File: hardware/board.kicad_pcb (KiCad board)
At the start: 2 copper layers, 65 x 140 mm, 25 parts, among them P1 CONN_4, P2 CONN_6, P3 CONN_6, Q1 BC547, U1 PIC16F628A, U2 7805

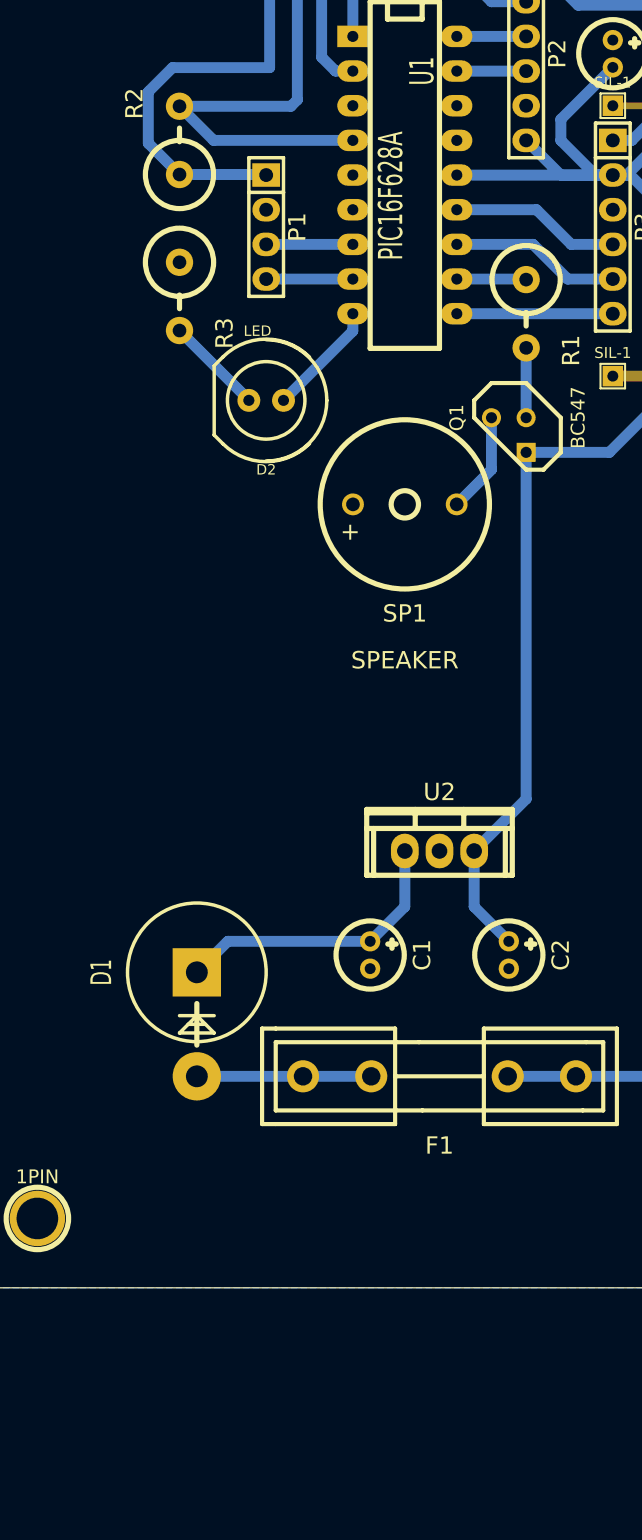
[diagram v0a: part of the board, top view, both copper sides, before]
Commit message: JZ: Label everything + ugly power tag workaround
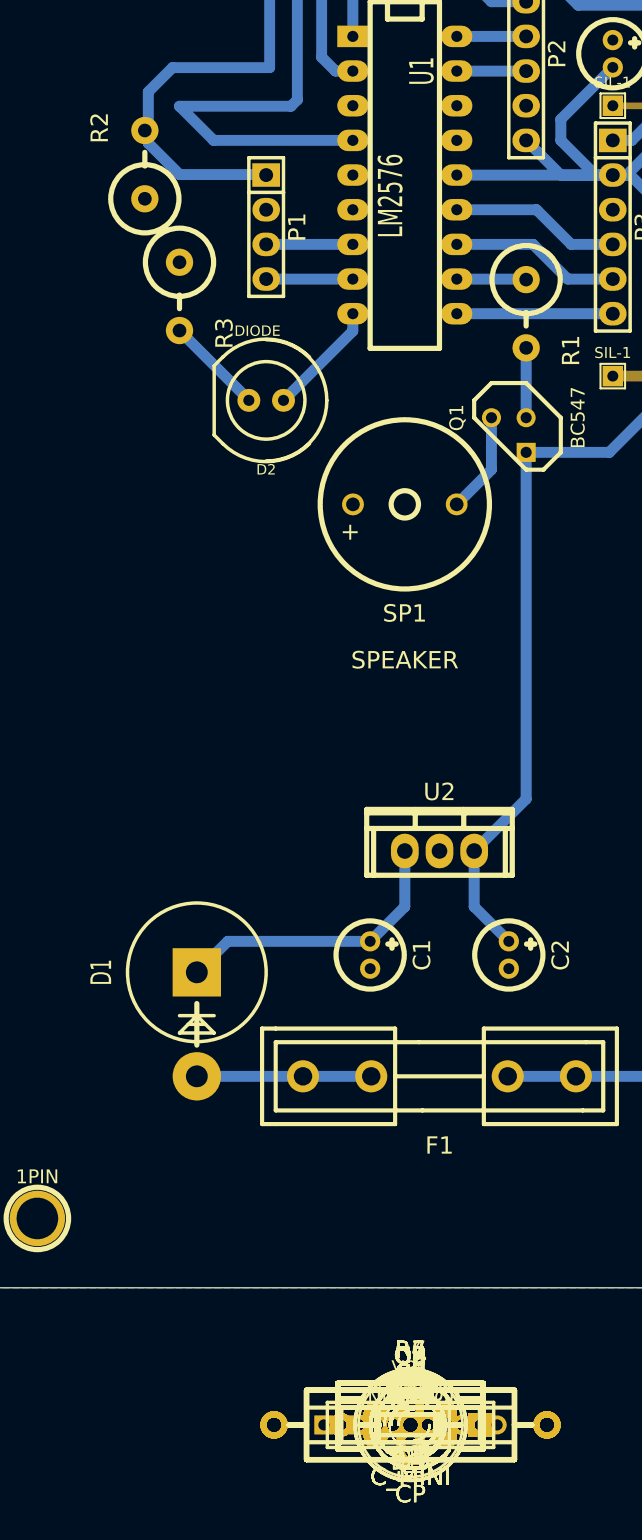
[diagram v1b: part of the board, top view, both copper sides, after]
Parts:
- added BT1: CONN_4, Connect:SIL-4, F.Cu at (147.7, 174.1)
- added C4, C5, C6, C7: C_MINI, Capacitors_ThroughHole:Capacitor5x11RM2.5, F.Cu at (147.7, 174.1)
- added C8, C9: CP, Capacitors_ThroughHole:Capacitor8x13RM3.8, F.Cu at (147.7, 174.1)
- added D10, D11, D12, D13, D14, D6, D7, D8, D9: LED, LEDs:LED-5MM, F.Cu at (147.7, 174.1)
- added D15, D16, D17, D18, D3, D4: DIODE, Diodes_ThroughHole:Diode_DO-35_SOD27_Horizontal_RM10, F.Cu at (147.7, 174.1)
- added D5: DIODESCH, Diodes_ThroughHole:Diode_DO-35_SOD27_Horizontal_RM10, F.Cu at (147.7, 174.1)
- added L1: INDUCTOR, Inductors:INDUCTOR_V, F.Cu at (147.7, 174.1)
- added Pickit3: CONN_6, Connect:SIL-6, F.Cu at (147.7, 174.1)
- added Q2, Q3, Q4, Q5: RFP50N06, Transistors_TO-220:TO-220_FET-GDS_Vertical_LargePads, F.Cu at (147.7, 174.1)
- added R4, R5, R6, R7: R, Resistors_ThroughHole:Resistor_Horizontal_RM20mm, F.Cu at (147.7, 174.1)
- added U3: LM7810ACT, Transistors_TO-220:TO-220_FET-GDS_Vertical_MountedFromLS_LargePads, F.Cu at (147.7, 174.1)
- added VR1: VR, Capacitors_ThroughHole:Capacitor12MMDiscRM7.75, F.Cu at (147.7, 174.1)
- C1: value 100nF -> 100uF
- C2: value 100nF -> 6800uF
- D1: value 1N007 -> DIODE
- D2: value LED -> DIODE
- F1: value 0.16A -> 1A
- P1: value CONN_4 -> SCREW TERM 1
- P2: value CONN_6 -> SCREW TERM 2
- P3: value CONN_6 -> SCREW TERM 3
- U1: value PIC16F628A -> LM2576
- U2: value 7805 -> PIC16F628A
- moved R2 3.10 mm to (128.3, 81.8)
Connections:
- C1 pad 1: N-000024 -> Net-(C1-Pad1)
- C1 pad 2: GND -> DGND
- C2 pad 2: GND -> DGND
- C3 pad 1: GND -> DGND
- D1 pad 1: N-000023 -> AGND
- D1 pad 2: N-000024 -> Net-(C1-Pad1)
- D2 pad 1: /LED -> Net-(D2-Pad1)
- D2 pad 2: N-000019 -> Net-(C1-Pad1)
- F1 pad 1: +12V -> /S0_I
- F1 pad 2: N-000023 -> Net-(D2-Pad1)
- P1 pad 1: +5V -> /S0_I
- P1 pad 2: GND -> /S0_O
- P1 pad 3: /P1_RX -> /S1_I
- P1 pad 4: /P1_TX -> (no net)
- P2 pad 1: N-000014 -> /S1_O
- P2 pad 2: N-000006 -> /S2_I
- P2 pad 3: N-000002 -> /S2_O
- P2 pad 4: N-000003 -> (no net)
- P2 pad 5: GND -> (no net)
- P2 pad 6: +5V -> (no net)
- P3 pad 1: /P3_1 -> /S3_I
- P3 pad 2: +5V -> /S3_O
- P3 pad 3: GND -> AGND
- P3 pad 4: /P3_4 -> (no net)
- P3 pad 5: /P3_5 -> (no net)
- P3 pad 6: /P3_6 -> (no net)
- R2 pad 2: /P3_1 -> /PK3_1
- R3 pad 1: GND -> DGND
- R3 pad 2: N-000019 -> Net-(D6-Pad2)
- SP1 pad 2: GND -> DGND
- U1 pad 1: N-000006 -> Net-(C1-Pad1)
- U1 pad 10: /P3_6 -> (no net)
- U1 pad 11: /BZR -> (no net)
- U1 pad 12: /P3_5 -> (no net)
- U1 pad 13: /P3_4 -> (no net)
- U1 pad 14: +5V -> (no net)
- U1 pad 17: N-000003 -> (no net)
- U1 pad 18: N-000002 -> (no net)
- U1 pad 2: N-000014 -> Net-(D5-Pad2)
- U1 pad 3: (no net) -> DGND
- U1 pad 4: /P3_1 -> +5V
- U1 pad 5: GND -> DGND
- U1 pad 7: /P1_RX -> (no net)
- U1 pad 8: /P1_TX -> (no net)
- U1 pad 9: /LED -> (no net)
- U2 pad GND: GND -> (no net)
- U2 pad VI: N-000024 -> (no net)
- U2 pad VO: +5V -> (no net)
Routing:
- net +5V: track 188.4 -> 96.6 mm
- net /PK3_1: track 0.00 -> 85.0 mm
- net /P3_1: track 77.3 -> 0.00 mm
- net /S3_I: track 0.00 -> 55.4 mm
- net (no net): track 0.00 -> 52.9 mm
- net Net-(C1-Pad1): track 0.00 -> 37.6 mm
- net N-000014: track 24.7 -> 0.00 mm
- net N-000024: track 23.1 -> 0.00 mm
- net /S3_O: track 0.00 -> 22.4 mm
- net /S0_I: track 0.00 -> 18.9 mm
- net N-000006: track 17.0 -> 0.00 mm
- net /S1_O: track 0.00 -> 15.4 mm
- net Net-(D2-Pad1): track 0.00 -> 13.5 mm
- net N-000023: track 12.8 -> 0.00 mm
- net +12V: track 12.5 -> 0.00 mm
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
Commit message: Heavily modded pcb + New footprint associations
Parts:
- removed 1PIN (x4): P***, Connect:1pin
- removed SIL-1 (x4): Val**, Connect:SIL-1
- removed SIL-2: Val**, Connect:SIL-2
- added IC1: PC817, opto:DIP-4__300, F.Cu at (210.8, 121.9)
- added IC2: PC817, opto:DIP-4__300, F.Cu at (198.1, 121.9)
- added IC3: PC817, opto:DIP-4__300, F.Cu at (232.4, 121.9)
- added IC4: PC817, opto:DIP-4__300, F.Cu at (219.7, 121.9)
- added IC5: PC817, opto:DIP-4__300, F.Cu at (222.2, 86.4)
- added IC6: PC817, opto:DIP-4__300, F.Cu at (234.9, 86.4)
- added IC7: PC817, opto:DIP-4__300, F.Cu at (200.7, 86.4)
- added IC8: PC817, opto:DIP-4__300, F.Cu at (213.4, 86.4)
- BT1: footprint Connect:SIL-4 -> Pin_Headers:Pin_Header_Straight_1x04
- C1: footprint Capacitors_Elko_ThroughHole:Elko_vert_DM5_RM2 -> Capacitors_ThroughHole:Capacitor10x25RM2.5
- C2: footprint Capacitors_Elko_ThroughHole:Elko_vert_DM5_RM2 -> Capacitors_ThroughHole:Capacitor16x25RM7.5
- C3: footprint Capacitors_Elko_ThroughHole:Elko_vert_DM5_RM2 -> Capacitors_ThroughHole:Capacitor3MMDiscRM2.5
- D1: footprint Diodes_ThroughHole:Diode_P600_Vertical_AnodeUp -> Diodes_ThroughHole:Diode_DO-41_SOD81_Vertical_AnodeUp
- D15, D16, D17, D18, D3, D4, D5: footprint Diodes_ThroughHole:Diode_DO-35_SOD27_Horizontal_RM10 -> Diodes_ThroughHole:Diode_DO-41_SOD81_Vertical_AnodeUp
- D2: footprint LEDs:LED-8MM -> Diodes_ThroughHole:Diode_DO-41_SOD81_Vertical_AnodeUp
- F1: footprint Fuse_Holders_and_Fuses:Fuseholder5x20_horiz_open_inline_Type-I -> Fuse_Holders_and_Fuses:Fuseholder5x20_horiz_SemiClosed_Casing10x25mm
- P1: footprint Pin_Headers:Pin_Header_Straight_1x04 -> moje's kicad footprints:Sawatronix_screwterm3
- P2, P3: footprint Pin_Headers:Pin_Header_Straight_1x06 -> moje's kicad footprints:Sawatronix_screwterm3
- Pickit3: footprint Connect:SIL-6 -> Pin_Headers:Pin_Header_Straight_1x06
- R1: footprint Resistors_ThroughHole:Resistor_Vertical_RM5mm -> Resistors_ThroughHole:Resistor_Horizontal_RM10mm
- R3: footprint Resistors_ThroughHole:Resistor_Vertical_RM5mm -> Resistors_ThroughHole:Resistor_Horizontal_RM15mm
- R4, R5, R6, R7: footprint Resistors_ThroughHole:Resistor_Horizontal_RM20mm -> Resistors_ThroughHole:Resistor_Vertical_RM5mm
- SP1: footprint Buzzers_Beepers:MagneticBuzzer_ProSignal_ABI-009-RC -> Buzzers_Beepers:MagneticBuzzer_ProSignal_ABT-410-RC
- U1: footprint Sockets_DIP:DIP-18__300_ELL -> Pentawatts:Pentawatt_Neutral_Straight_Vertical_TO220-5-T05A
- U2: footprint moje's kicad footprints:78XX -> Sockets_DIP:DIP-18__300_ELL
- U3: value LM7810ACT -> LM7810; footprint Transistors_TO-220:TO-220_FET-GDS_Vertical_MountedFromLS_LargePads -> moje's kicad footprints:78XX
- VR1: footprint Capacitors_ThroughHole:Capacitor12MMDiscRM7.75 -> Capacitors_ThroughHole:Capacitor6MMDiscRM5
- moved D17 129.3 mm to (234.9, 78.7)
- moved Q4 129.2 mm to (227.3, 72.4)
- moved C6 124.2 mm to (227.3, 78.7), turned to 270 degrees
- moved Q5 117.1 mm to (205.7, 72.4)
- moved D12 115.8 mm to (233.7, 96.5), turned to 270 degrees
- moved D18 115.8 mm to (213.4, 78.7)
- moved P1 114.9 mm to (246.4, 121.9)
- moved R6 113.9 mm to (227.3, 92.7), turned to 270 degrees
- moved C7 111.6 mm to (205.7, 78.7), turned to 270 degrees
- moved D11 106.7 mm to (221.0, 96.5), turned to 90 degrees
- moved D9 106.2 mm to (233.7, 111.8), turned to 270 degrees
- moved D14 100.8 mm to (212.1, 96.5), turned to 270 degrees
- moved R7 100.0 mm to (205.7, 92.7), turned to 270 degrees
- moved L1 99.4 mm to (173.4, 78.1)
- moved R5 98.8 mm to (227.3, 115.6), turned to 90 degrees
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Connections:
- C8 pad 1: Net-(C8-Pad1) -> /S0_I
- Q2 pad D: (no net) -> /S0_I
- Q2 pad G: (no net) -> Net-(IC1-Pad4)
- Q2 pad S: (no net) -> /S0_O
- Q3 pad D: (no net) -> /S1_I
- Q3 pad G: (no net) -> Net-(IC3-Pad4)
- Q3 pad S: (no net) -> /S1_O
- Q4 pad D: (no net) -> /S2_I
- Q4 pad G: (no net) -> Net-(IC5-Pad4)
- Q4 pad S: (no net) -> /S2_O
- Q5 pad D: (no net) -> /S3_I
- Q5 pad G: (no net) -> Net-(IC7-Pad4)
- Q5 pad S: (no net) -> /S3_O
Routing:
- net AGND: track 7.78 -> 275.8 mm, vias 0 -> 4
- net +5V: track 96.6 -> 300.0 mm
- net +10V: track 0.00 -> 179.7 mm
- net /S0_I: track 18.9 -> 164.2 mm, vias 0 -> 2
- net /S0_O: track 0.00 -> 113.9 mm
- net /S1_O: track 15.4 -> 80.6 mm
- net (no net): track 52.9 -> 0.00 mm
- net /S2_O: track 0.00 -> 51.5 mm
- net /S2_I: track 2.54 -> 52.9 mm
- net /CSW_2: track 0.00 -> 45.4 mm
- net /CSW_1: track 0.00 -> 45.4 mm
- net /S3_O: track 22.4 -> 66.7 mm
- net /PK3_1: track 85.0 -> 50.0 mm, vias 0 -> 2
- net Net-(D2-Pad1): track 13.5 -> 47.9 mm
- net Net-(IC7-Pad4): track 0.00 -> 33.0 mm
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- added copper zone on B.Cu, net AGND
- added copper zone on B.Cu, net DGND
- removed copper zone on B.Cu, net GND
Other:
- board outline removed
- net class Default: clearance 0.25 -> 0.4; trace_width 0.8 -> 0.75
- rule trace_clearance: 0.25 -> 0.4
- board text removed: "mrmoje.github.io"

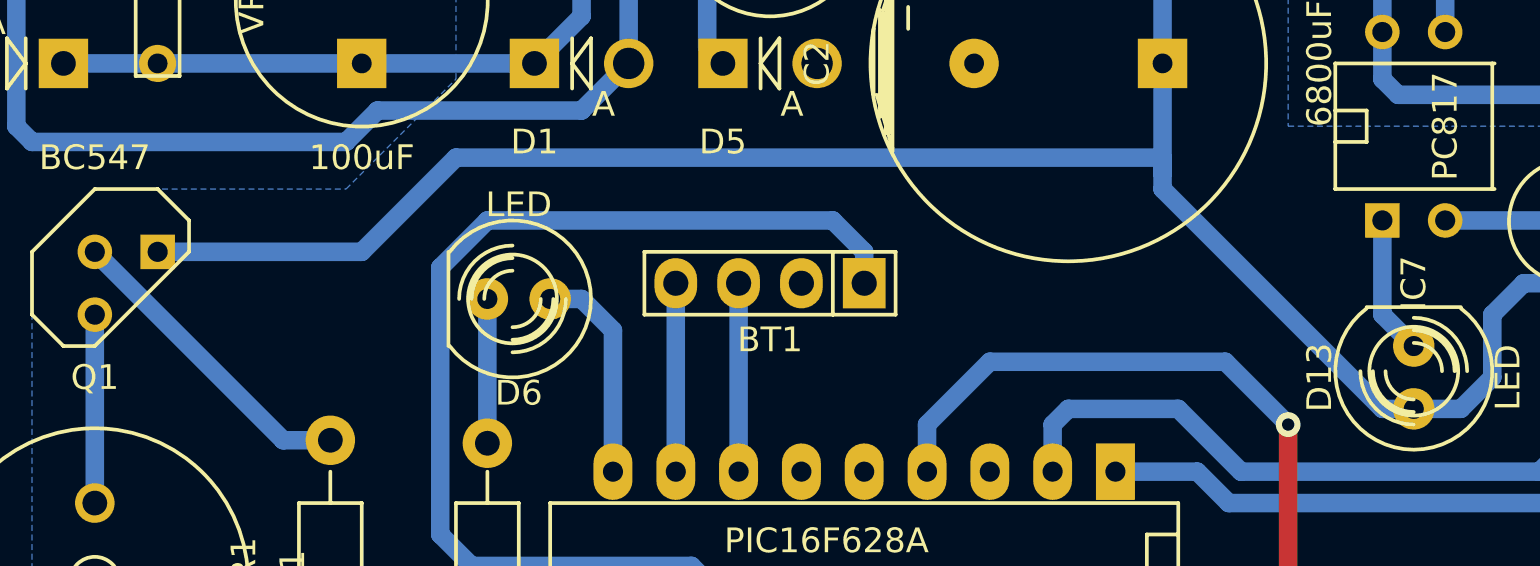
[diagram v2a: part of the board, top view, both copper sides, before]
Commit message: Forgot to connect power trace to uC & bt modules
Discovered after second etch [facepalm]
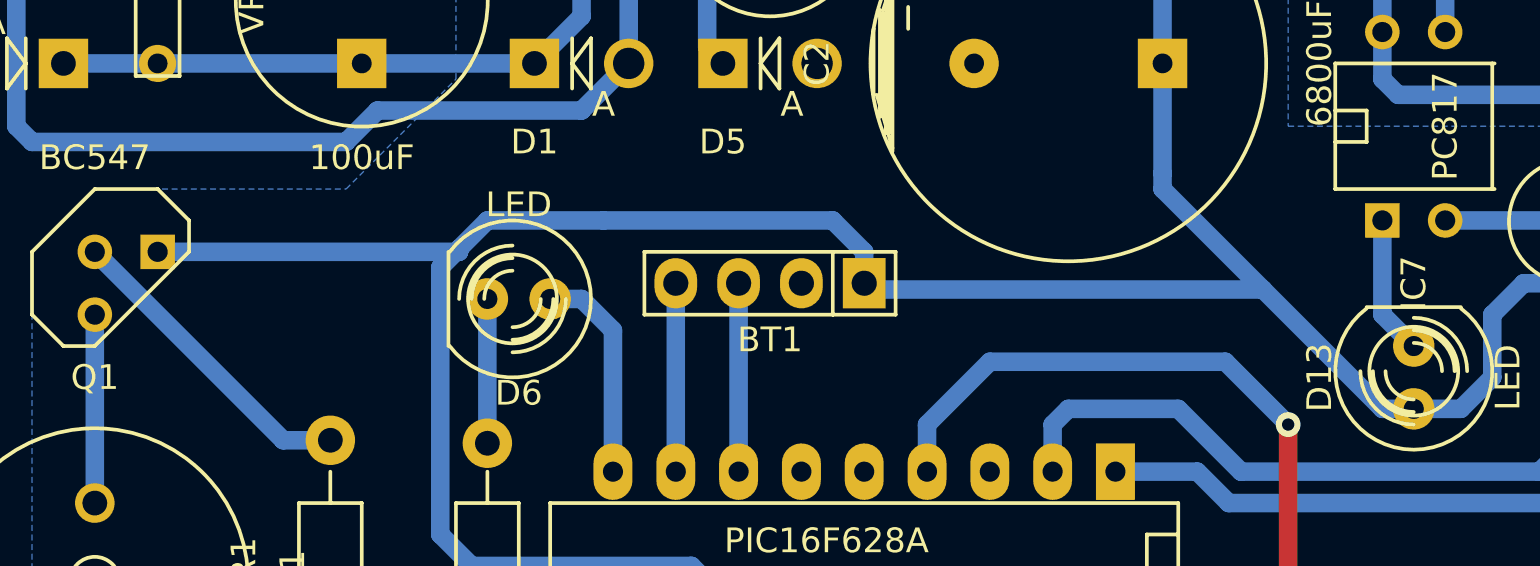
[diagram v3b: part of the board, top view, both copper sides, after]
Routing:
- net +5V: track 300.0 -> 285.7 mm
